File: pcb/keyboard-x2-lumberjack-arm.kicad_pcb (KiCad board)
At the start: 2 copper layers, 285 x 94.2 mm, 141 parts, among them J1 16-pin USB-C Connector SMD, U1 STM32F103 Bluepill, or MiniF4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, U2 SN74LVC1T45DBV

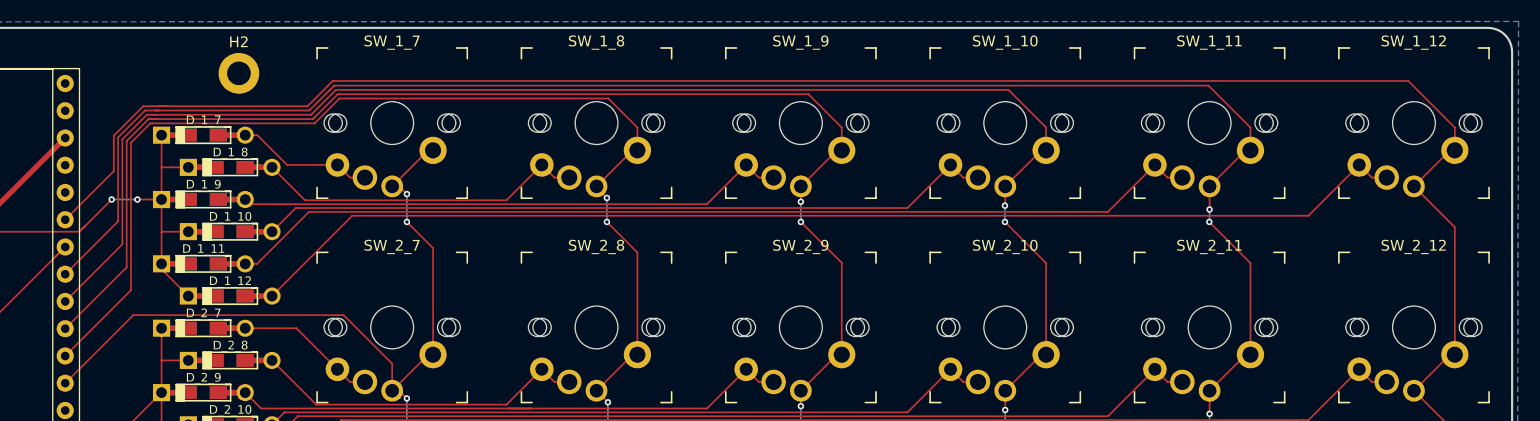
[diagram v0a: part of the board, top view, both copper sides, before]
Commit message: feat: 1U hotswap sw1-7 - sw1-12
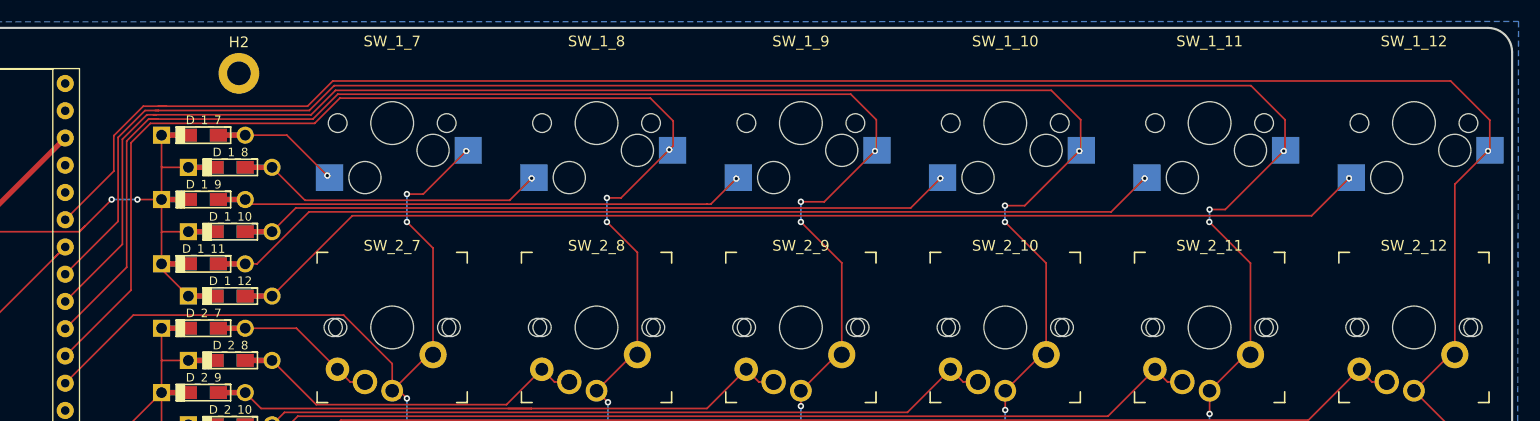
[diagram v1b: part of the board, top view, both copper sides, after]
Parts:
- SW_1_10, SW_1_11, SW_1_12, SW_1_7, SW_1_8, SW_1_9: footprint ProjectLocal:SW_MX_PG1350_NoLed -> ProjectLocal:MXOnly-1U-Hotswap-180
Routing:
- net /COL9: track 187.6 -> 193.8 mm, vias 10 -> 11
- net /COL10: track 204.3 -> 210.3 mm, vias 10 -> 11
- net /COL11: track 221.5 -> 227.3 mm, vias 10 -> 11
- net /COL8: track 169.7 -> 174.9 mm, vias 10 -> 11
- net Net-(D_1_9-Pad2): track 51.4 -> 47.3 mm, vias 0 -> 1
- net Net-(D_1_8-Pad2): track 30.8 -> 26.7 mm, vias 0 -> 1
- net Net-(D_1_12-Pad2): track 109.5 -> 105.4 mm, vias 0 -> 1
- net Net-(D_1_10-Pad2): track 68.9 -> 64.8 mm, vias 0 -> 1
- net Net-(D_1_11-Pad2): track 91.7 -> 87.6 mm, vias 0 -> 1
- net Net-(D_1_7-Pad2): track 12.8 -> 9.68 mm, vias 0 -> 1
- net /COL12: track 236.6 -> 238.4 mm, vias 0 -> 1
- net /COL7: track 135.7 -> 136.4 mm, vias 10 -> 11

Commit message: feat: 1U hotswap sw2-1 - sw2-12
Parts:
- SW_2_1, SW_2_10, SW_2_11, SW_2_12, SW_2_2, SW_2_3, SW_2_4, SW_2_5, SW_2_6, SW_2_7, SW_2_8, SW_2_9: footprint ProjectLocal:SW_MX_PG1350_NoLed -> ProjectLocal:MXOnly-1U-Hotswap-180
- moved D5 7.82 mm to (68.7, 87.4)
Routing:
- net /5V: track 210.5 -> 202.2 mm
- net VBUS: track 28.2 -> 35.1 mm
- net Net-(D_2_9-Pad2): track 54.1 -> 50.0 mm, vias 0 -> 1
- net Net-(D_2_8-Pad2): track 31.3 -> 27.2 mm, vias 0 -> 1
- net Net-(D_2_12-Pad2): track 109.0 -> 105.0 mm, vias 0 -> 1
- net Net-(D_2_10-Pad2): track 68.4 -> 64.4 mm, vias 0 -> 1
- net Net-(D_2_11-Pad2): track 91.2 -> 87.2 mm, vias 0 -> 1
- net /COL9: track 193.8 -> 197.7 mm, vias 11 -> 12
- net /COL3: track 181.2 -> 184.9 mm, vias 11 -> 12
- net /COL10: track 210.3 -> 214.0 mm, vias 11 -> 12
- net /COL11: track 227.3 -> 230.8 mm, vias 11 -> 12
- net /COL2: track 203.1 -> 206.6 mm, vias 11 -> 12
- net /COL1: track 230.6 -> 233.9 mm, vias 11 -> 12
- net Net-(D_2_7-Pad2): track 13.2 -> 10.1 mm, vias 0 -> 1
- net /COL7: track 136.4 -> 139.4 mm, vias 11 -> 12
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
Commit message: feat: 1U hotswap sw3-1 - sw3-12
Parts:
- SW_3_1, SW_3_10, SW_3_11, SW_3_12, SW_3_2, SW_3_3, SW_3_4, SW_3_5, SW_3_6, SW_3_7, SW_3_8, SW_3_9: footprint ProjectLocal:SW_MX_PG1350_NoLed -> ProjectLocal:MXOnly-1U-Hotswap-180
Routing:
- net Net-(D_3_9-Pad2): track 52.3 -> 48.3 mm, vias 0 -> 1
- net Net-(D_3_8-Pad2): track 31.7 -> 27.7 mm, vias 0 -> 1
- net Net-(D_3_12-Pad2): track 108.6 -> 104.5 mm, vias 0 -> 1
- net Net-(D_3_10-Pad2): track 68.0 -> 64.0 mm, vias 0 -> 1
- net Net-(D_3_11-Pad2): track 90.8 -> 86.7 mm, vias 0 -> 1
- net /COL2: track 206.6 -> 210.3 mm, vias 12 -> 13
- net /COL10: track 214.0 -> 217.7 mm, vias 12 -> 13
- net /COL11: track 230.8 -> 234.3 mm, vias 12 -> 13
- net Net-(D_3_7-Pad2): track 13.7 -> 10.5 mm, vias 0 -> 1
- net /COL4: track 165.6 -> 168.4 mm, vias 12 -> 13
- net /COL3: track 184.9 -> 187.7 mm, vias 12 -> 13
- net /COL9: track 197.7 -> 200.4 mm, vias 12 -> 13
- net /COL8: track 177.5 -> 180.1 mm, vias 12 -> 13
- net /COL5: track 147.9 -> 150.3 mm, vias 12 -> 13
- net /COL6: track 125.3 -> 127.7 mm, vias 12 -> 13
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
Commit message: feat: 1U hotswap sw4-1 - sw4-12
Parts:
- SW_4_1, SW_4_10, SW_4_11, SW_4_12, SW_4_2, SW_4_3, SW_4_4, SW_4_5, SW_4_6, SW_4_7, SW_4_8, SW_4_9: footprint ProjectLocal:SW_MX_PG1350_NoLed -> ProjectLocal:MXOnly-1U-Hotswap-180
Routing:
- net Net-(D_4_9-Pad2): track 52.7 -> 48.5 mm, vias 0 -> 1
- net Net-(D_4_10-Pad2): track 68.4 -> 64.1 mm, vias 0 -> 1
- net Net-(D_4_11-Pad2): track 90.6 -> 86.3 mm, vias 0 -> 1
- net Net-(D_4_12-Pad2): track 108.2 -> 103.9 mm, vias 0 -> 1
- net Net-(D_4_8-Pad2): track 32.1 -> 28.1 mm, vias 0 -> 1
- net /COL10: track 217.7 -> 221.4 mm, vias 13 -> 14
- net /COL3: track 187.7 -> 191.4 mm, vias 13 -> 14
- net /COL11: track 234.3 -> 237.8 mm, vias 13 -> 14
- net /COL1: track 235.9 -> 239.4 mm, vias 13 -> 14
- net /COL9: track 200.4 -> 203.2 mm, vias 13 -> 14
- net /COL4: track 168.4 -> 171.1 mm, vias 13 -> 14
- net /COL8: track 180.1 -> 182.6 mm, vias 13 -> 14
- net /COL5: track 150.3 -> 152.8 mm, vias 13 -> 14
- net /COL2: track 210.3 -> 212.8 mm, vias 13 -> 14
- net /COL6: track 127.7 -> 129.9 mm, vias 13 -> 14
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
